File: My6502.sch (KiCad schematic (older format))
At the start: 40 parts, among them J1 ~NMI, J2 Aux 5VDC, J3 Power 5V, J4 Expansion Bus, J5 Port A, J6 Port B, J7 GND, SW1 RESET, U1 WD65C02, U2 ROM 28C256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

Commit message: YAsicfive02 1.5 final version - Gerber file done
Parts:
- J2: footprint (none) -> Connector_PinHeader_2.54mm:PinHeader_1x03_P2.54mm_Vertical
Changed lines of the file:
@@
 encoding utf-8
 Sheet 1 1
-Title ""
-Date ""
-Rev ""
-Comp ""
+Title "YAsixfive02 SBC"
+Date "2022-10-07"
+Rev "1.5"
+Comp "(c) Mariano Luna"
 Comment1 ""
 Comment2 ""
@@
 F 0 "J2" V 10850 5050 50  0000 L CNN
 F 1 "Aux 5VDC" V 10950 4950 50  0000 L CNN
-F 2 "" H 11000 5100 50  0001 C CNN
+F 2 "Connector_PinHeader_2.54mm:PinHeader_1x03_P2.54mm_Vertical" H 11000 5100 50  0001 C CNN
 F 3 "~" H 11000 5100 50  0001 C CNN
 	1    11000 5100
@@
 Wire Wire Line
 	10150 5400 10150 5650
-Wire Bus Line
-	5550 6900 5550 7300
-Wire Bus Line
-	4350 7000 4350 7450
-Wire Bus Line
-	3300 6900 3300 7300
-Wire Bus Line
-	2100 7000 2100 7450
-Wire Bus Line
-	6650 5500 6650 6700
-Wire Bus Line
-	3100 3200 3100 3800
-Wire Bus Line
-	5300 3750 5300 4550
-Wire Bus Line
-	3450 5100 3450 5850
-Wire Bus Line
-	3350 4250 3350 5050
-Wire Bus Line
-	5300 4850 5300 5650
-Wire Bus Line
-	2050 4450 2050 5250
-Wire Bus Line
-	5550 1250 5550 2050
-Wire Bus Line
-	7950 1100 7950 1900
-Wire Bus Line
-	3200 2400 3200 3150
-Wire Bus Line
-	1100 2400 1100 3800
-Wire Bus Line
-	4200 1350 4200 2850
-Wire Bus Line
-	6550 1100 6550 2600
-Wire Bus Line
-	950  4750 950  6350
 $Comp
 L Connector:Conn_01x01_Male J7
@@
 	1    0    0    -1
 $EndComp
+Wire Bus Line
+	5550 6900 5550 7300
+Wire Bus Line
+	4350 7000 4350 7450
+Wire Bus Line
+	3300 6900 3300 7300
+Wire Bus Line
+	2100 7000 2100 7450
+Wire Bus Line
+	6650 5500 6650 6700
+Wire Bus Line
+	3100 3200 3100 3800
+Wire Bus Line
+	5300 3750 5300 4550
+Wire Bus Line
+	3450 5100 3450 5850
+Wire Bus Line
+	3350 4250 3350 5050
+Wire Bus Line
+	5300 4850 5300 5650
+Wire Bus Line
+	2050 4450 2050 5250
+Wire Bus Line
+	5550 1250 5550 2050
+Wire Bus Line
+	7950 1100 7950 1900
+Wire Bus Line
+	3200 2400 3200 3150
+Wire Bus Line
+	1100 2400 1100 3800
+Wire Bus Line
+	4200 1350 4200 2850
+Wire Bus Line
+	6550 1100 6550 2600
+Wire Bus Line
+	950  4750 950  6350
 $EndSCHEMATC

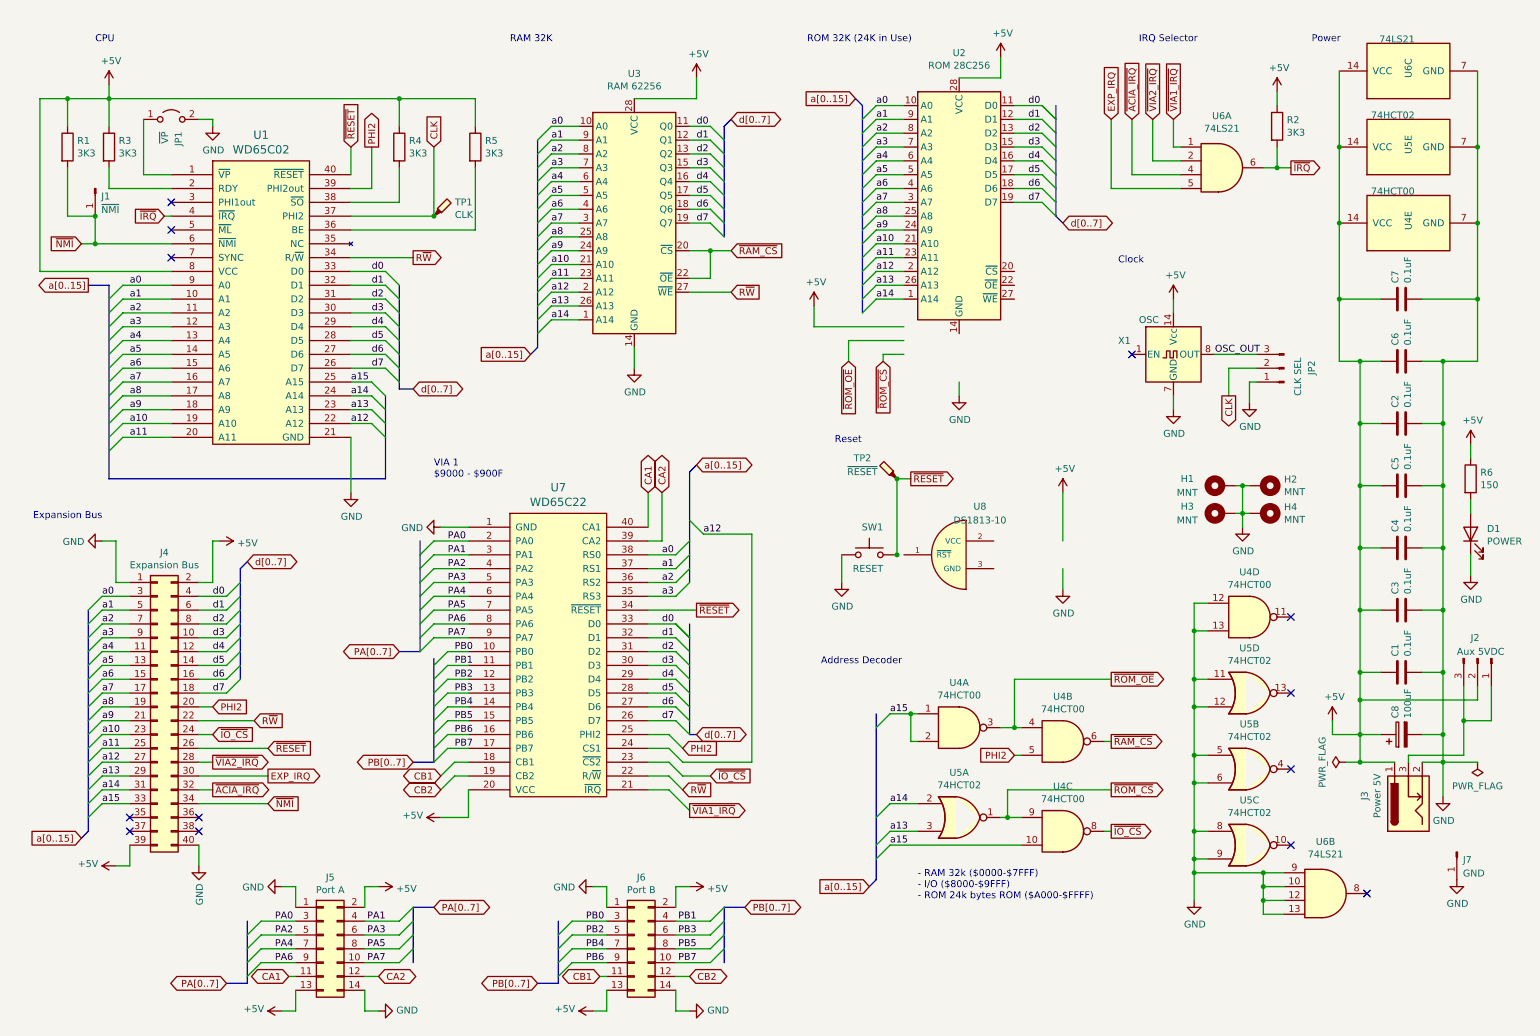
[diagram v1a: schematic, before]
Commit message: Added ACIA in schematic
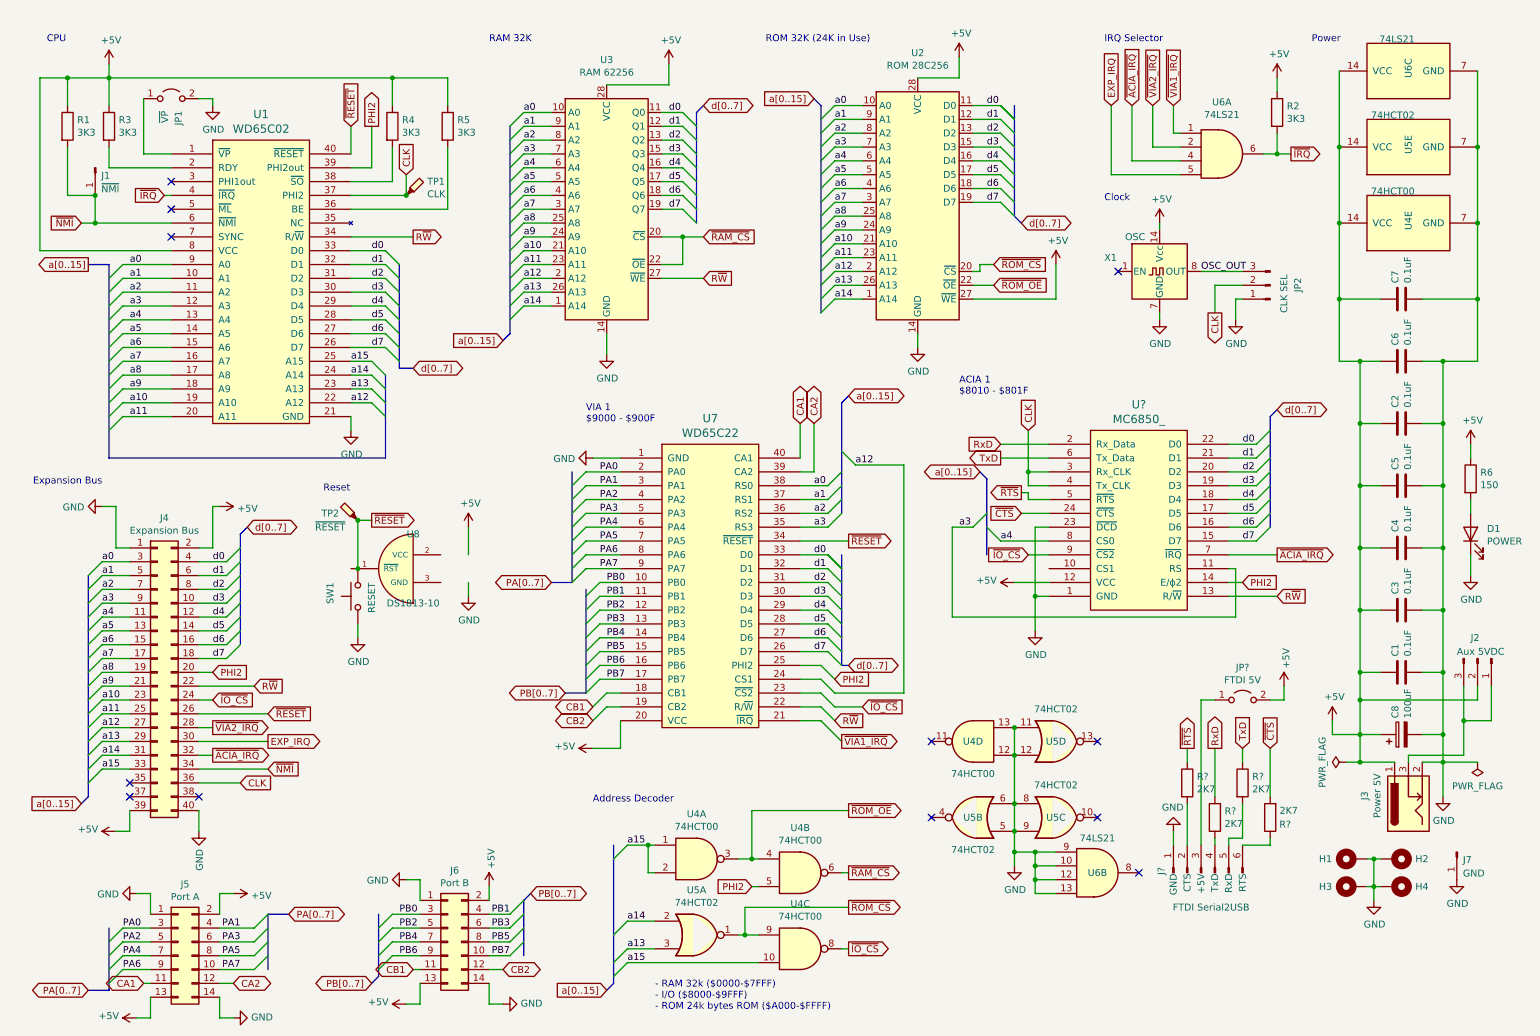
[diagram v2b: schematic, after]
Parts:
- added J?: FTDI Serial2USB, Connector_PinHeader_2.54mm:PinHeader_1x06_P2.54mm_Vertical, symbol Connector:FTDI_Conn_01x06_Male
- added JP?: FTDI 5V, Connector_PinHeader_2.54mm:PinHeader_2x01_P2.54mm_Vertical, symbol Jumper:Jumper_2_Open
- added R? (x4): 2K7, Resistor_THT:R_Axial_DIN0207_L6.3mm_D2.5mm_P10.16mm_Horizontal, symbol Device:R
- added U?: MC6850_, symbol 65xx:MC6850_
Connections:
- net +5V: now also U2.27 (~WE), JP?.2 (B), U?.12 (VCC)
- net CLK: now also J4.36 (Pin_36), U?.3 (Rx_CLK), U?.4 (Tx_CLK)
- net GND: now also U2.14 (GND), J?.1 (GND), U?.1 (GND), U?.23 (~DCD)
- net PHI2: now also U?.14 (E/ϕ2)
- net R~W: now also U?.13 (R/~W)
- net a3: now also U?.11 (RS)
- net a4: now also U?.8 (CS0)
- net d0: now also U?.22 (D0)
- net d1: now also U?.21 (D1)
- net d2: now also U?.20 (D2)
- net d3: now also U?.19 (D3)
- net d4: now also U?.18 (D4)
- net d5: now also U?.17 (D5)
- net d6: now also U?.16 (D6)
- net d7: now also U?.15 (D7)
- net ~ACIA_IRQ: now also U?.7 (~IRQ)
- net ~IO_CS: now also U?.9 (~CS2)
- net ~ROM_CS: now also U2.20 (~CS)
- net ~ROM_OE: now also U2.22 (~OE)
- new net: J?.2 (CTS), R?.2
- new net: J?.3 (+5V), JP?.1 (A)
- new net: J?.4 (TxD), R?.2
- new net: J?.5 (RxD), R?.2
- new net: J?.6 (RTS), R?.1
- new net RxD: R?.1, U?.2 (Rx_Data)
- new net TxD: R?.1, U?.6 (Tx_Data)
- new net ~CTS: R?.2, U?.24 (~CTS)
- new net ~RTS: R?.1, U?.5 (~RTS)
- no-connect marks 13 -> 12
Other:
- note added: "ACIA 1\n$8010 - $801F"
- moved on the sheet: H1, H2, H3, H4, J1, J4, J5, J6, JP1, JP2, R1, R2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

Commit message: c1.5.2 schematic finished - error in U9 oin 23
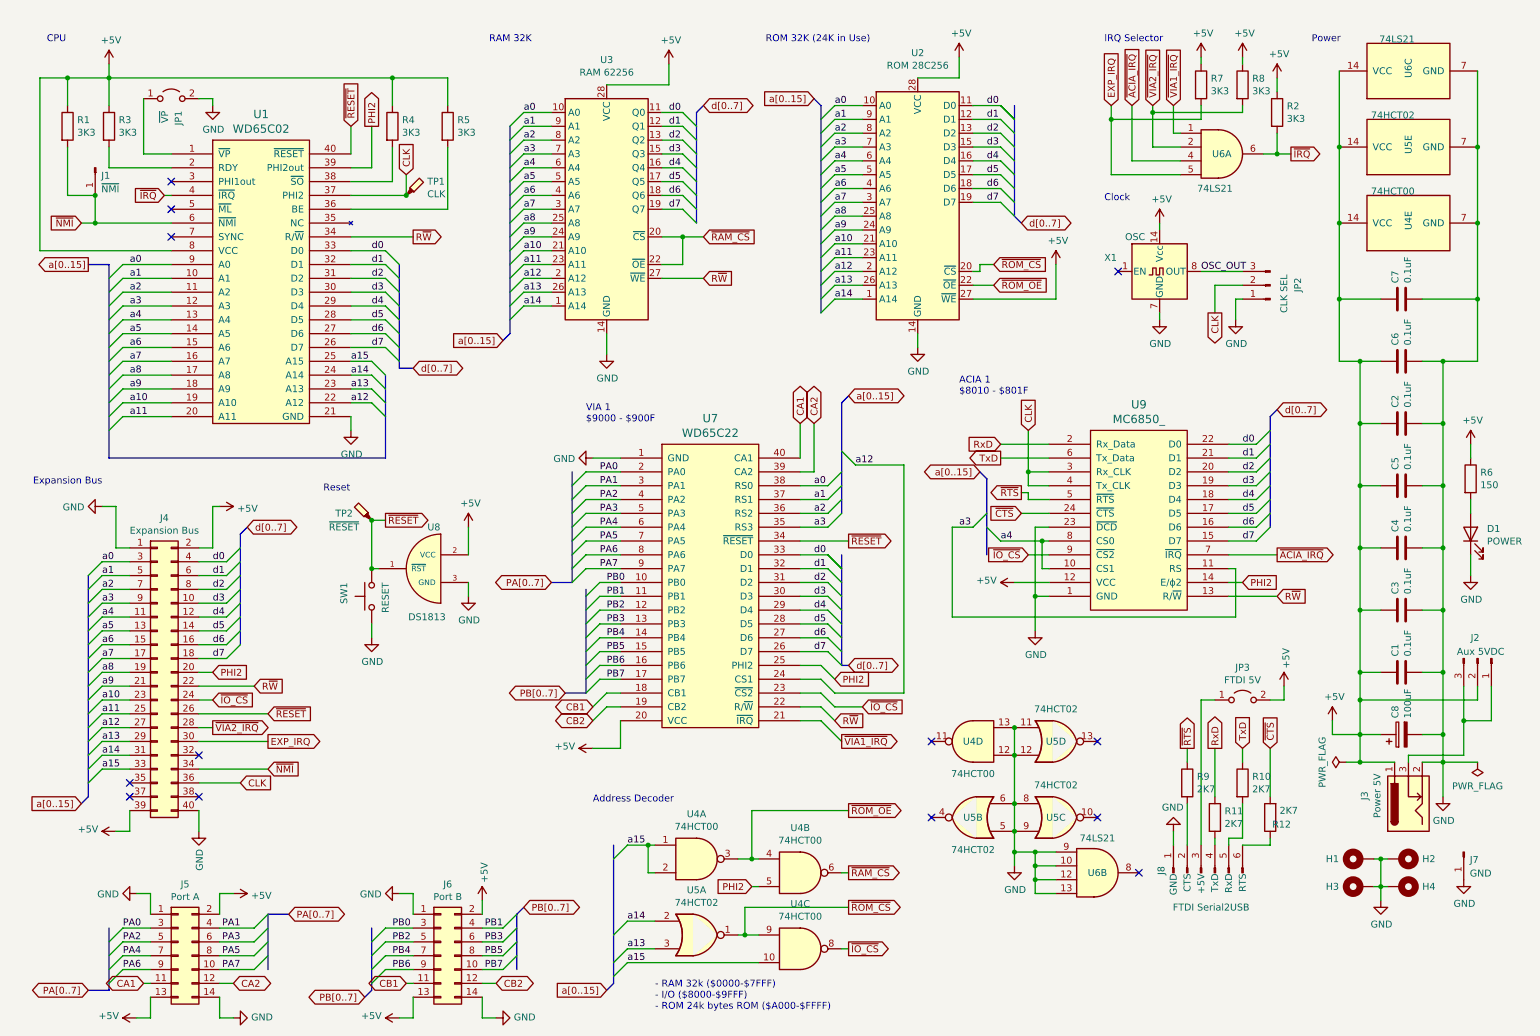
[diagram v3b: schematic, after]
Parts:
- added R7, R8: 3K3, Resistor_THT:R_Axial_DIN0207_L6.3mm_D2.5mm_P10.16mm_Horizontal, symbol Device:R
- U8: value DS1813-10 -> DS1813
- gave numbers to parts that had none: 7
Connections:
- net +5V: now also U8.2 (VCC), R7.1, R8.1
- net EXP_IRQ: now also R7.2
- net GND: now also U8.3 (GND)
- net a4: now also U9.10 (CS1)
- net ~ACIA_IRQ: no longer J4.32 (Pin_32)
- net ~RESET: now also U8.1 (~RST)
- net ~VIA2_IRQ: now also R8.2
- no-connect marks 12 -> 13
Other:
- moved on the sheet: H1, H2, H3, H4, J6, J7, SW1, TP2, U8

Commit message: Schema ready v1.5.2 ACIA and VIA on
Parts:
- U9: footprint (none) -> Package_DIP:DIP-24_W15.24mm_LongPads
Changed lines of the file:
@@
 F 0 "U9" H 8550 4937 60  0000 C CNN
 F 1 "MC6850_" H 8550 4831 60  0000 C CNN
-F 2 "" H 8550 3450 60  0000 C CNN
+F 2 "Package_DIP:DIP-24_W15.24mm_LongPads" H 8550 3450 60  0000 C CNN
 F 3 "" H 8550 3450 60  0000 C CNN
 	1    8550 4100
@@
 Wire Wire Line
 	7850 4450 7850 4250
+Connection ~ 7850 4250
+Wire Wire Line
+	7850 4250 7550 4250
 Wire Bus Line
 	7450 3800 7450 4350
@@
 Wire Bus Line
 	950  4500 950  6100
-Connection ~ 7850 4250
-Wire Wire Line
-	7850 4250 7550 4250
 $EndSCHEMATC

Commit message: PCB Component placement first take
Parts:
- renumbered R6 to R1, R1 to R2, R2 to R6
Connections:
- net Aux_0v: now reaches J2.1 (Pin_1), J2.3 (Pin_3), J3.3
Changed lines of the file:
@@
 ~IRQ
 $Comp
-L Device:R R1
+L Device:R R2
 U 1 1 6121736C
 P 800 1250
-F 0 "R1" H 870 1296 50  0000 L CNN
+F 0 "R2" H 870 1296 50  0000 L CNN
 F 1 "3K3" H 870 1205 50  0000 L CNN
 F 2 "Resistor_THT:R_Axial_DIN0207_L6.3mm_D2.5mm_P10.16mm_Horizontal" V 730 1250 50  0001 L CNN
@@
 	1900 4000 1850 4000
 $Comp
-L Device:R R2
+L Device:R R6
 U 1 1 6125C994
 P 9550 1150
-F 0 "R2" H 9620 1196 50  0000 L CNN
+F 0 "R6" H 9620 1196 50  0000 L CNN
 F 1 "3K3" H 9620 1105 50  0000 L CNN
 F 2 "Resistor_THT:R_Axial_DIN0207_L6.3mm_D2.5mm_P10.16mm_Horizontal" V 9480 1150 50  0001 L CNN
@@
 $EndComp
 $Comp
-L Device:R R6
+L Device:R R1
 U 1 1 64B58252
 P 10950 3800
-F 0 "R6" H 11020 3846 50  0000 L CNN
+F 0 "R1" H 11020 3846 50  0000 L CNN
 F 1 "150" H 11020 3755 50  0000 L CNN
 F 2 "Resistor_THT:R_Axial_DIN0207_L6.3mm_D2.5mm_P10.16mm_Horizontal" V 10880 3800 50  0001 L CNN
@@
 F 0 "U9" H 8550 4937 60  0000 C CNN
 F 1 "MC6850_" H 8550 4831 60  0000 C CNN
-F 2 "Package_DIP:DIP-24_W15.24mm_LongPads" H 8550 3450 60  0000 C CNN
+F 2 "Package_DIP:DIP-24_W15.24mm_LongPads" H 8550 3450 60  0001 C CNN
 F 3 "" H 8550 3450 60  0000 C CNN
 	1    8550 4100
@@
 Wire Bus Line
 	950  4500 950  6100
+Text Label 10950 5550 0    50   ~ 0
+Aux_0v
 $EndSCHEMATC
